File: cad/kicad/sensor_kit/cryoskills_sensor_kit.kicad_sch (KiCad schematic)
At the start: 48 parts, among them J1 PWR_In, J10 QWIIC_I2C_2, J11 DS18B20, J12 SERIAL_BREAKOUT, J13 USB_B, J2 PWR_SENSE_Panel, J3 PWR_SENSE_Battery, J4 Adalogger_3V3, J5 Adalogger_VBUS, J6 Adalogger_RegulatorEN, J7 PT1000_RTD_WHEAT, J8 SPI_BREAKOUT, J9 QWIIC_I2C_1, SW1 SPDT Switch, SW2 SW_Push, U1 RFM96W, U4 FT231XQ

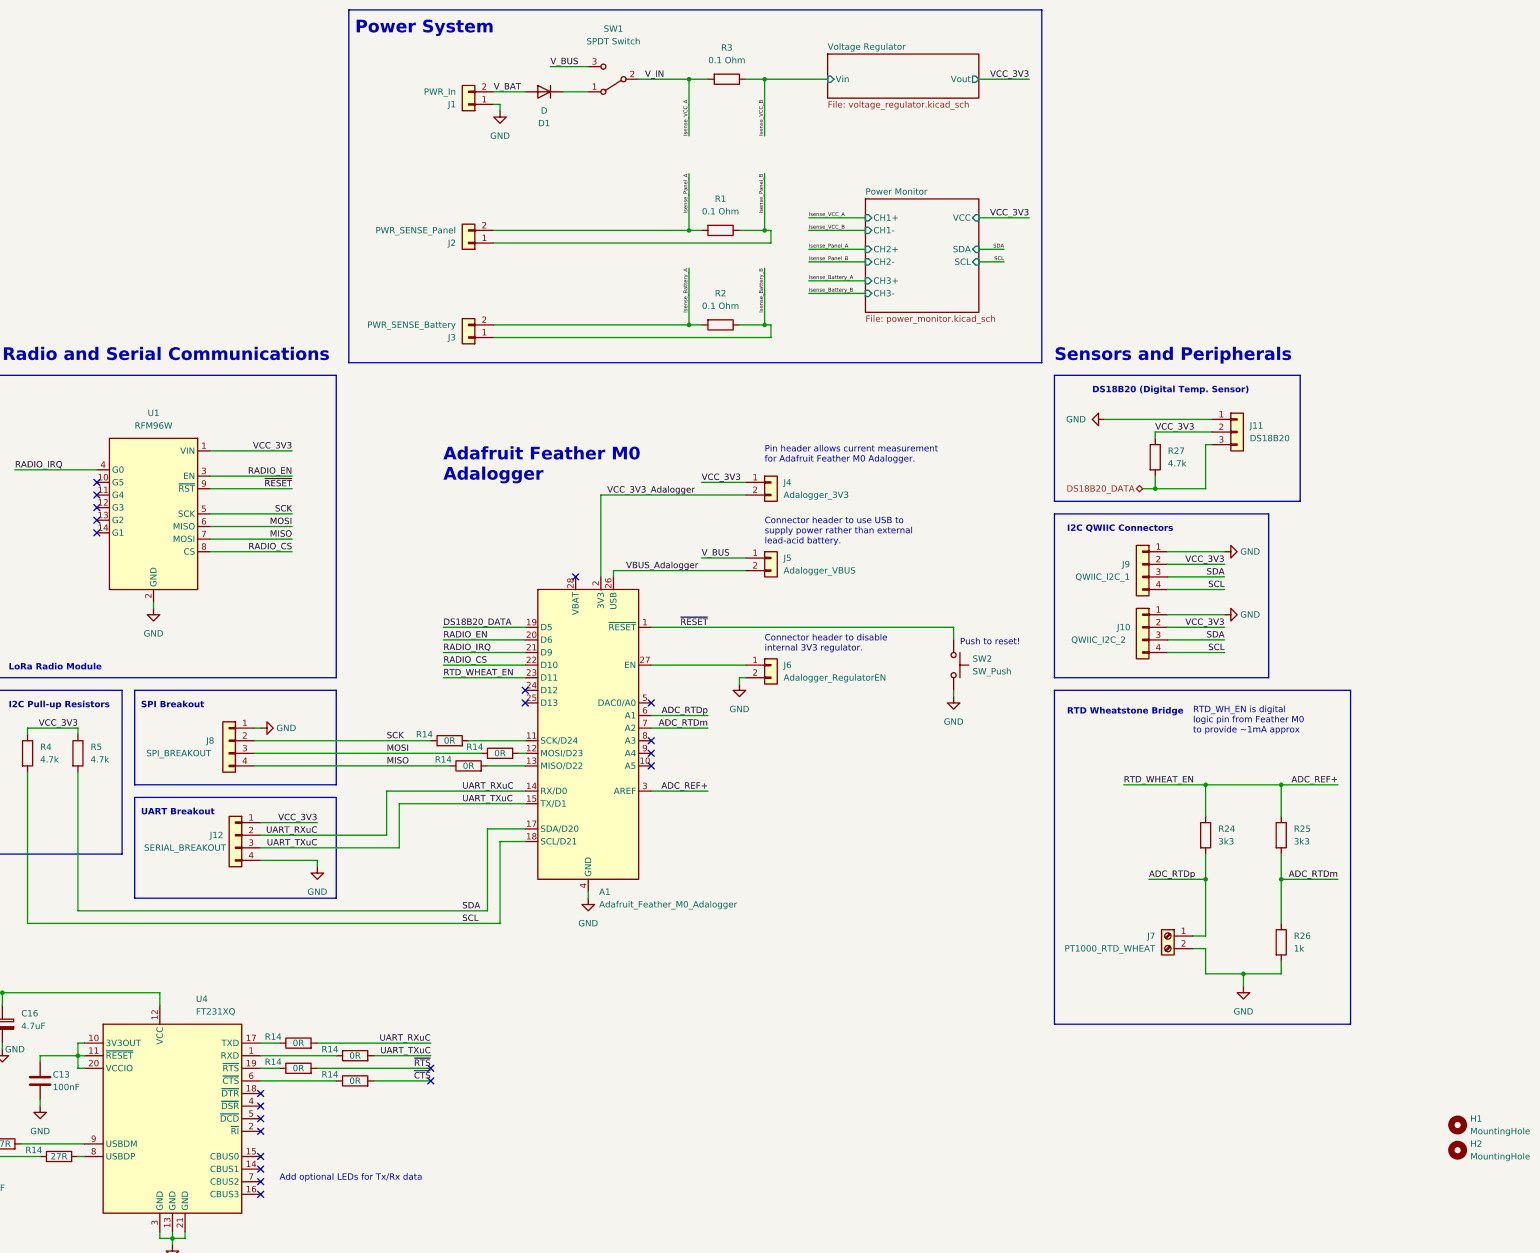
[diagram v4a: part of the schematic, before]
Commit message: fixes MISO/MOSI on RFM96, swaps Dp/Dm on USB and makes pads for THT resistors bigger
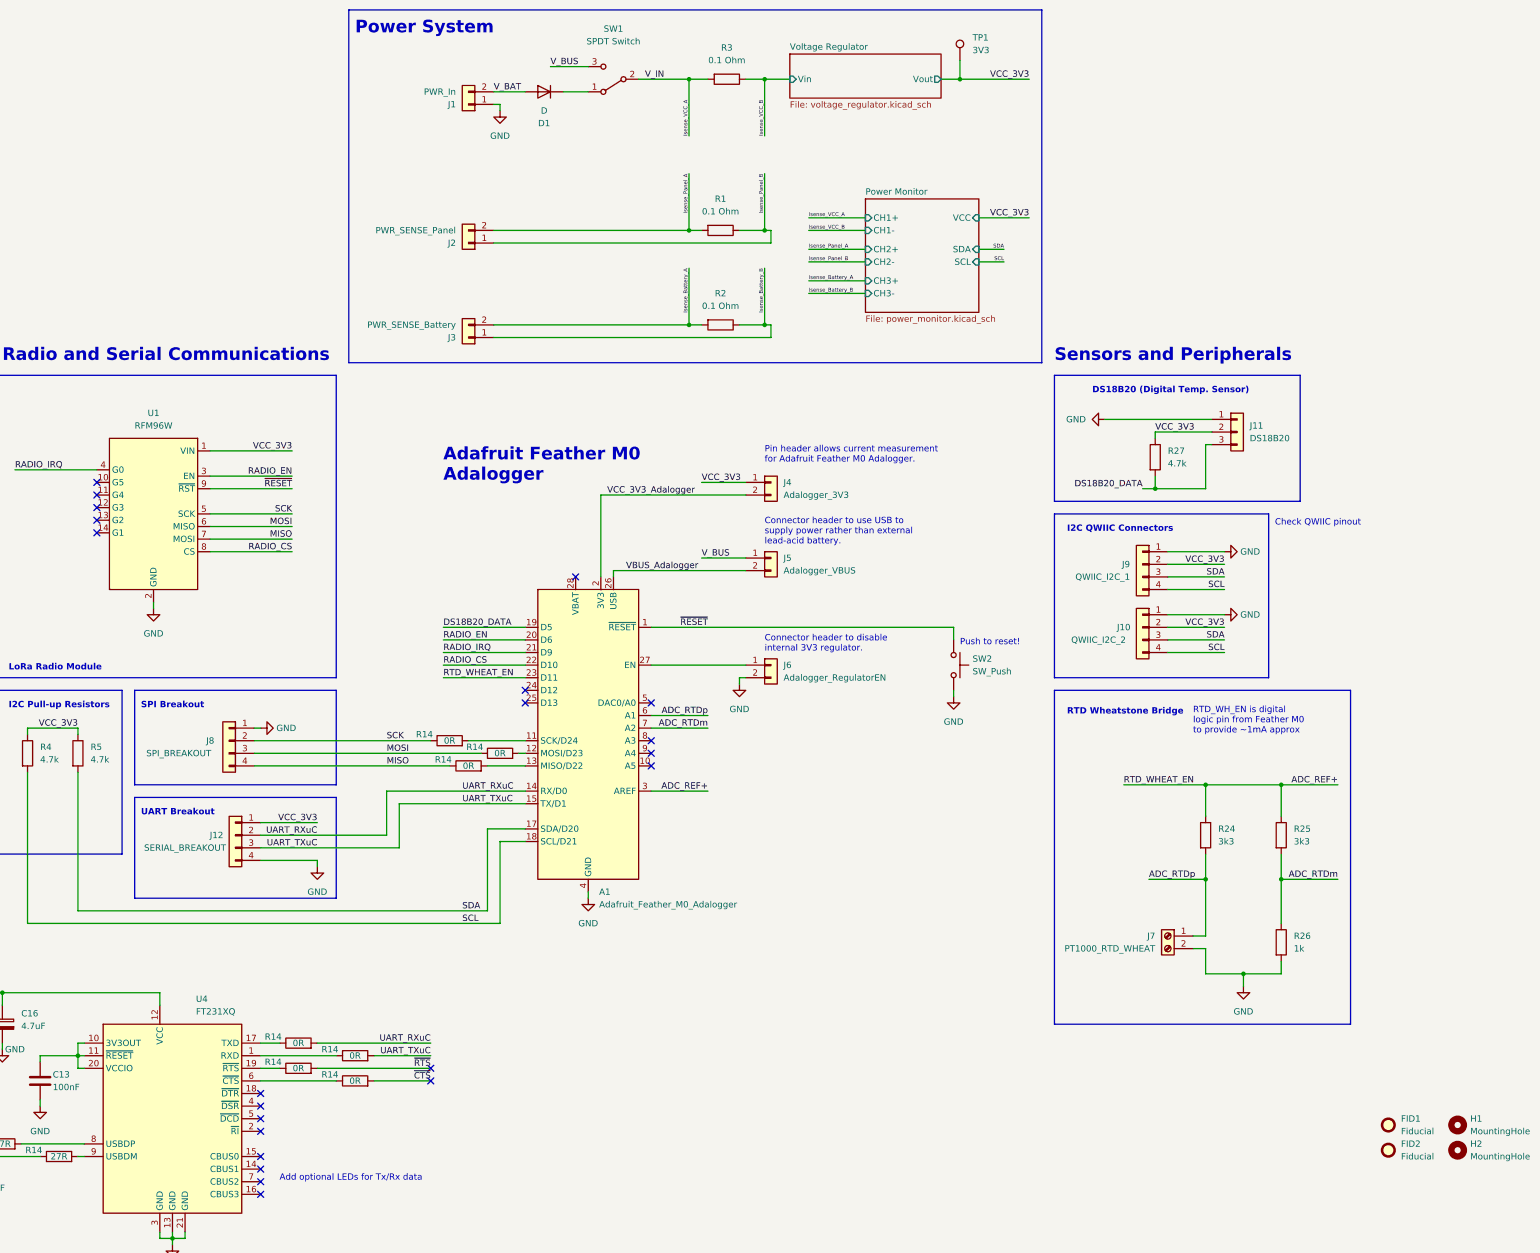
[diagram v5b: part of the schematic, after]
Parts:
- added FID1, FID2: Fiducial, Fiducial:Fiducial_1mm_Mask2mm, symbol Mechanical:Fiducial
- added TP1: 3V3, TestPoint:TestPoint_Pad_D2.0mm, symbol Connector:TestPoint
- A1, J1, J2, J3, U1: Placed (none) -> No; now left out of the parts list
- C11, C12: Manufacturer (none) -> Multicomp Pro; MftrPartNo (none) -> MC0402N470J500CT; Placed (none) -> Yes; Supplier (none) -> Farnell; SupplierPartNo (none) -> 1758959
- C13, C15: Manufacturer (none) -> Multicomp Pro; MftrPartNo (none) -> MC0402N101J500CT; Placed (none) -> Yes; Supplier (none) -> Farnell; SupplierPartNo (none) -> 1758969
- C14: Manufacturer (none) -> Multicomp Pro; MftrPartNo (none) -> MCU0603R103KCT; Placed (none) -> Yes; Supplier (none) -> Farnell; SupplierPartNo (none) -> 9406182
- C16: footprint (none) -> Capacitor_SMD:C_0603_1608Metric; Manufacturer (none) -> Murata; MftrPartNo (none) -> GRT188R61C475KE13D; Placed (none) -> Yes; Supplier (none) -> Farnell; SupplierPartNo (none) -> 3581438
- D1: Manufacturer (none) -> Multicomp Pro; MftrPartNo (none) -> SS13B; Placed (none) -> Yes; Supplier (none) -> Farnell; SupplierPartNo (none) -> 1861425
- FB1: Manufacturer (none) -> Abracon; MftrPartNo (none) -> AFBC-Q0603-301-T; Placed (none) -> Yes; Supplier (none) -> Farnell; SupplierPartNo (none) -> 4141767
- H1, H2, H3, H4: footprint MountingHole:MountingHole_3.2mm_M3 -> MountingHole:MountingHole_5.3mm_M5; Placed (none) -> No; now left out of the parts list
- J10, J9: Manufacturer (none) -> JST; MftrPartNo (none) -> SM04B-SRSS-TB(LF)(SN); Placed (none) -> Yes; Supplier (none) -> Farnell; SupplierPartNo (none) -> 1830839
- J11: Manufacturer Multicomp PRO -> Multicomp Pro; Placed (none) -> No; SupplierPartNo 4179098 -> 4179099; now left out of the parts list
- J12, J8: Manufacturer (none) -> Multicomp Pro; MftrPartNo (none) -> 2211S-04G; Placed (none) -> No; Supplier (none) -> Farnell; SupplierPartNo (none) -> 1593413
- J13: Manufacturer (none) -> GCT; MftrPartNo (none) -> USB3076-30-A; Placed (none) -> Yes; Supplier (none) -> Farnell; SupplierPartNo (none) -> 2443117
- J4, J5, J6: Manufacturer (none) -> Multicomp Pro; MftrPartNo (none) -> 2211S-02G; Placed (none) -> No; Supplier (none) -> Farnell; SupplierPartNo (none) -> 1593411
- J7: Manufacturer Multicomp PRO -> Multicomp Pro; Placed (none) -> No; now left out of the parts list
- R1, R2, R3: Manufacturer (none) -> TE Connectivity; MftrPartNo (none) -> RLC73K2BR10FTDF; Placed (none) -> Yes; Supplier (none) -> Farnell; SupplierPartNo (none) -> 4173948
- R14: Manufacturer (none) -> Multicomp Pro; MftrPartNo (none) -> MCWR08X0000FTL; Placed (none) -> Yes; Supplier (none) -> Farnell; SupplierPartNo (none) -> 2747563
- R14: Manufacturer (none) -> Multicomp Pro; MftrPartNo (none) -> MCWR04X27R0FTL; Placed (none) -> Yes; Supplier (none) -> Farnell; SupplierPartNo (none) -> 2447146
- R24, R25, R26: MftrPartNo (none) -> DNF; Placed (none) -> No; now left out of the parts list
- R27: MftrPartNo (none) -> DNF; Placed (none) -> No
- R4, R5: Manufacturer (none) -> Multicomp Pro; MftrPartNo (none) -> MCWF08P4701FTL; Placed (none) -> Yes; Supplier (none) -> Farnell; SupplierPartNo (none) -> 2694141
- SW1, SW2: Placed (none) -> No
- U4: Manufacturer (none) -> FTDI; MftrPartNo (none) -> FT231XQ; Placed (none) -> Yes; Supplier (none) -> Farnell; SupplierPartNo (none) -> 2081330
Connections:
- net VCC_3V3: now also TP1.1
- net at R14.2: now also U4.9 (USBDM); no longer U4.8 (USBDP)
- net at R14.2: now also U4.8 (USBDP); no longer U4.9 (USBDM)
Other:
- note added: "Check QWIIC pinout"

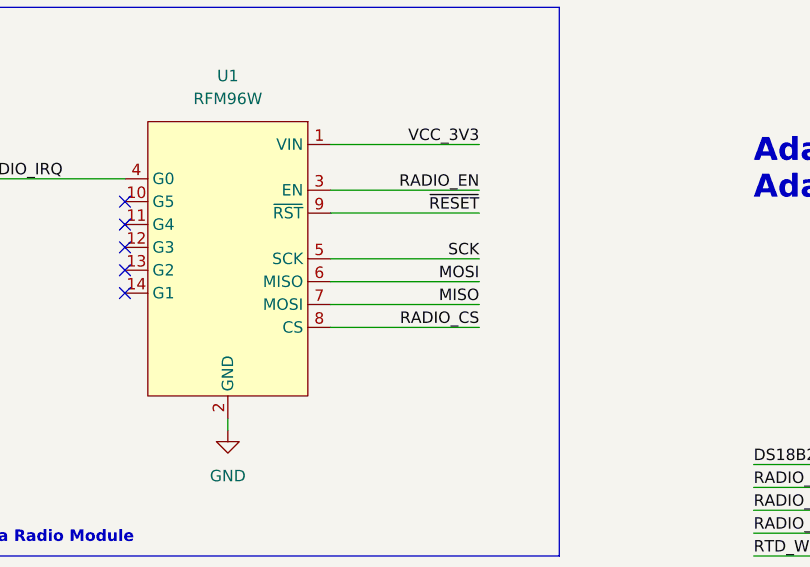
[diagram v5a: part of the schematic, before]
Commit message: corrects MISO/MIMO silkscreen labels
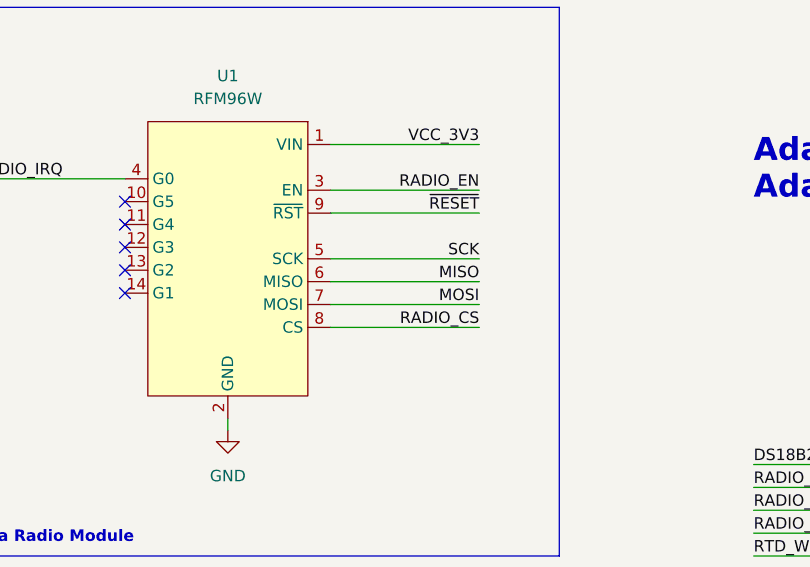
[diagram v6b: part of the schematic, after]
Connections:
- net MISO: now also U1.6 (MISO); no longer U1.7 (MOSI)
- net MOSI: now also U1.7 (MOSI); no longer U1.6 (MISO)
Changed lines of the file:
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@@
-    (stroke (width 0) (type default))
-  )
-  (wire (pts (xy 135.89 123.19) (xy 119.38 123.19))
     (stroke (width 0) (type default))
   )
@@
     (stroke (width 0) (type default))
   )
+  (wire (pts (xy 119.38 123.19) (xy 135.89 123.19))
+    (stroke (width 0) (type default))
+  )
   (wire (pts (xy 215.9 63.5) (xy 215.9 52.07))
     (stroke (width 0) (type default))
@@
     (stroke (width 0) (type default))
   )
-  (wire (pts (xy 135.89 125.73) (xy 119.38 125.73))
-    (stroke (width 0) (type default))
-  )
   (wire (pts (xy 335.28 175.26) (xy 346.71 175.26))
     (stroke (width 0) (type default))
@@
   )
   (wire (pts (xy 190.5 35.56) (xy 195.58 35.56))
+    (stroke (width 0) (type default))
+  )
+  (wire (pts (xy 119.38 125.73) (xy 135.89 125.73))
     (stroke (width 0) (type default))
   )
@@
     (effects (font (size 1.27 1.27)) (justify left bottom))
   )
-  (label "MISO" (at 135.89 125.73 180) (fields_autoplaced)
+  (label "MISO" (at 135.89 123.19 180) (fields_autoplaced)
     (effects (font (size 1.27 1.27)) (justify right bottom))
   )
@@
     (effects (font (size 1.27 1.27)) (justify left bottom))
   )
-  (label "MOSI" (at 135.89 123.19 180) (fields_autoplaced)
-    (effects (font (size 1.27 1.27)) (justify right bottom))
-  )
+  (label "MOSI" (at 135.89 125.73 180) (fields_autoplaced)
+    (effects (font (size 1.27 1.27)) (justify right bottom))
+  )

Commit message: updates production files from sensor kit materials
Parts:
- added R: 1k, Resistor_THT:R_Axial_DIN0204_L3.6mm_D1.6mm_P5.08mm_Horizontal, symbol Device:R
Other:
- note added: "'Net labels' indicate that two or more points are connected without a wire being drawn!"
- note added: "------------------------- Any components that are highlighted with an orange box and background do not comefitted to the PCB and you will need to solder these yourself. Check them off the schematic as you go to make sure you've done all of them!"
- note added: "------------------------- The power system allows you to select between using the 12V battery, or the 5V supply from the USB to power your instrument. The 5V supply is helpful for when you are testing functionality on the circuit board."
- note added: "---------------------------- KiCAD requires that you include mechanical features of the circuit, such as mounting holes and fiducial marks (for alignment of the PCB during manufacture) on the schematic. This is used to tell the PCB editor what sized hole or marking should be used."
- note added: "---------------------------------------- The Adafruit Feather M0 Adalogger is the 'brain' of the sensor kit and is responsible for the timing of measurements, reading values from the temperature sensors and writing these to an SD card."
- note added: "------------------------------------------------------------ The USB DEBUG port provides an additional USB serial port for the sensor kit which can still be used when the Adalogger is not powered by its USB connection, or when you are using the Adalogger in SLEEP mode."
- note added: "12V Batt. Powered and External Regulator"
- note added: "12V Battery Input"
- note added: "3V3 or 0V"
- note added: "A B"
- note added: "A1 (ADC_RTDp) is the analogue input if the PT1000 is used in a potential divider. A2 (ADC_RTDm) can be used with in addition to A1 if the PT1000 is used in a Wheatstone bridge configuration."
- note added: "Adalogger Header Configurations"
- note added: "Battery voltage and current Panel voltage and current 3V3 regulator voltage and current"
- note added: "C D"
- note added: "CH1 CH2 CH3"
- note added: "Connect the PT1000 here - orientation of the red/white wires does not matter!"
- note added: "Control pins for the RFM96 radio module."
- note added: "Current sensing resistors"
- note added: "DATA pin of the DS18B20 temperature sensor"
- note added: "Digital output to apply 0V or 3V3 to PT1000 circuit."
- note added: "E F"
- note added: "Exposes the SPI interface for testing and extension purposes."
- note added: "Exposes the UART (USB DEBUG) interface for testing and extension purposes."
- note added: "INA3221 Power Monitor"
- note added: "J4 J5 J6 POWER SWITCH"
- note added: "JUMPER CONNECTED JUMPER CONNECTED JUMPER DISCONNECTED USB"
- note added: "JUMPER CONNECTED JUMPER DISCONNECTED JUMPER DISCONNECTED BATT."
- note added: "JUMPER DISCONNECTED JUMPER DISCONNECTED JUMPER DISCONNECTED OFF"
- note added: "Jumper resistors to RS-232 interface"
- note added: "Jumper resistors to SPI interface"
- note added: "Mechanical Symbols"
- note added: "OPTIONAL: Wheatstone Bridge"
- note added: "PCB Soldering Help"
- note added: "POTENTIAL DIVIDER"
- note added: "PT1000 Temperature Interface"
- note added: "RADIO_EN (Pin 6) must be HIGH/3V3 for radio to work!"
- note added: "RFM96W (LoRa) Radio Module"
- note added: "RTD (PT1000) Potential Divider / Wheatstone Bridge"
- note added: "RTD_WHEAT_EN is digital output (Pin 11) which applies a value of 3V3 or 0V from the Adalogger. The value(s) of R24 (and optionally R25, R26) should limit the maximum current to approximately 1mA to avoid self heating of the PT1000 temperature sensor."
- note added: "Reverse protection diode"
- note added: "SPI interface is used for communication between the Adalogger and the RFM96W radio modules."
- note added: "The DATA line of the DS18B20 temperature sensoris connected to Pin D5 on the Adalogger."
- note added: "The DS18B20 will not work without R27 (4.7k) soldered between the DATA and 3V3 pins!"
- note added: "This block hides the 3.3V voltage regulator circuitry!"
- note added: "This block hides the voltage regulator circuitry!"
- note added: "This circuitry is taken from the FT21XQ datasheet (Section 6.1) https://ftdichip.com/wp-content/uploads/2021/10/DS_FT231X.pdf"
- note added: "USB Debug Port"
- note added: "USB Powered (Adalogger Only)"
- note added: "USB Powered and External Regulator"
- note added: "Using a second potential divider with fixed resistors and measuring the voltage difference of (ADC_RTDp - ADC_RTDm) is known as a Wheatstone Bridge and can be used to improve sensitivity and resolution of the PT1000 temperature sensor."
- note added: "V"
- note added: "WHEATSTONE"
- note added: "_EN = Enable _IRQ = Interupt _CS = Chip Select"
- note removed: "Check QWIIC pinout"
- note removed: "LoRa Radio Module"
- note removed: "RTD Wheatstone Bridge"
- note removed: "RTD_WH_EN is digital logic pin from Feather M0 to provide ~1mA approx"
- company: Cardiff University -> Cardiff University & CryoSkills Organising Committee
- moved on the sheet: A1, C11, C12, C13, C14, C15, C16, D1, FB1, FID1, FID2, H1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
